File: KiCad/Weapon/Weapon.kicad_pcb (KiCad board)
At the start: 2 copper layers, 97.3 x 61 mm, 34 parts, among them IC1 ATMEGA328-P, J1 MICRO_USB, P1 2P_CGRID_M, P2 USB-TTL, P3 2P_CGRID_M, Q1 NPN, Q2 NPN, U1 MCP73831, U2 RFID-RC522, U3 LM1084IT-3.3/NOPB, X1 16MHz

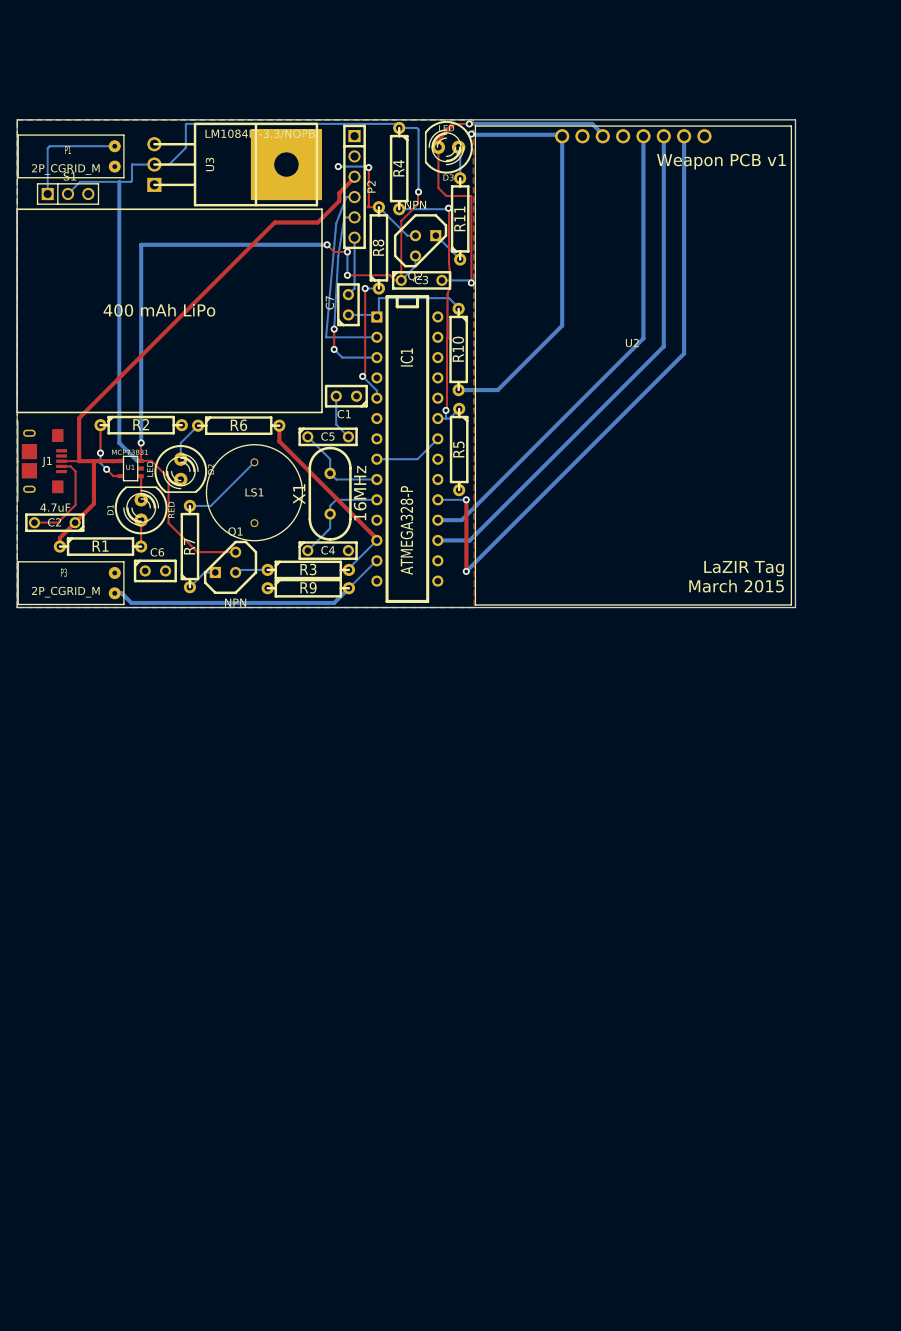
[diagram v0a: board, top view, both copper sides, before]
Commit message: Revert "3/29 KiCad Updates"
This reverts commit a2529da1b40b1f6e0e832ed1976ed3be41434859.
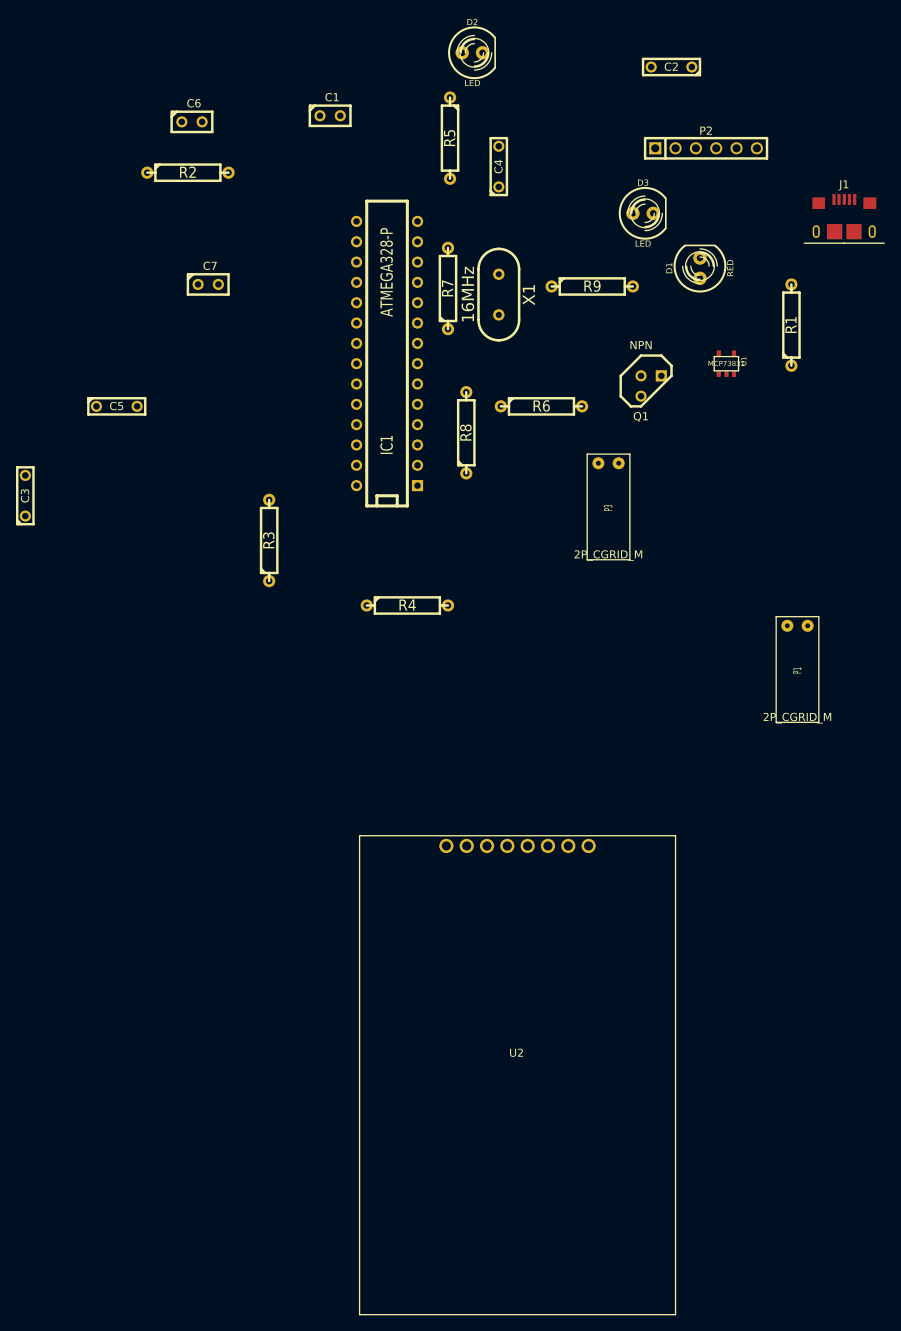
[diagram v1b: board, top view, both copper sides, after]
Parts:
- removed LS1: BUZZER, AI-1223Buzzer
- removed Q2: NPN, TO92
- removed R10: 10k, R4
- removed R11: 330, R4
- removed S1: SLIDESWITCH, PIN_ARRAY_3X1
- removed U3: LM1084IT-3.3/NOPB, TO220
- R3, R8: value 560 -> 10k
- R5: value 10k -> 1k
- R6: value 1k -> 560
- R7: value 330 -> 10k
- R9: value 10k -> 330
- moved J1 105.8 mm to (135.6, 37.8), turned to 0 degrees
- moved P1 103.6 mm to (129.8, 87.1), turned to 0 degrees
- moved C2 95.8 mm to (114.0, 17.3)
- moved R1 90.7 mm to (129.0, 49.5), turned to 90 degrees
- moved U2 89.9 mm to (114.6, 173.2)
- moved D1 76.1 mm to (117.6, 42.4)
- moved U1 75.6 mm to (120.9, 54.4), turned to 0 degrees
- moved D2 63.6 mm to (89.2, 15.5), turned to 0 degrees
- moved P3 63.5 mm to (106.2, 66.8), turned to 0 degrees
- moved Q1 57.6 mm to (111.5, 57.1), turned to 0 degrees
- moved C3 56.4 mm to (33.3, 70.9), turned to 90 degrees
- moved C6 56.3 mm to (54.1, 24.1)
- moved R4 54.6 mm to (81.0, 84.6), turned to 0 degrees
- moved C4 52.5 mm to (92.5, 29.7), turned to 90 degrees
- moved R9 51.8 mm to (104.1, 44.7)
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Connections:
- C3 pad 2: GND -> (no net)
- D2 pad 1: N-0000017 -> N-0000018
- IC1 pad 12: LED/Buzzer -> StatusLED
- P1 pad 2: N-000001 -> V-Bat
- Q1 pad 1: N-0000013 -> N-0000042
- Q1 pad 2: N-0000012 -> N-0000041
- R2 pad 2: GND -> (no net)
- R3 pad 1: N-0000012 -> V-Bat
- R3 pad 2: LED/Buzzer -> VoltageSense
- R4 pad 1: V-Bat -> VoltageSense
- R4 pad 2: VoltageSense -> GND
- R5 pad 1: VoltageSense -> N-0000018
- R5 pad 2: GND -> StatusLED
- R6 pad 1: N-0000017 -> LED-Driver
- R6 pad 2: LED/Buzzer -> N-0000041
- R7 pad 1: N-0000013 -> GND
- R7 pad 2: N-0000014 -> Trigger
- R8 pad 1: LED-Driver -> Reset
- R8 pad 2: N-0000042 -> +3.3V
- R9 pad 1: GND -> N-0000042
- R9 pad 2: Trigger -> N-0000043
- U1 pad 2: GND -> (no net)
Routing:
- net V-Bat: track 193.4 -> 0.00 mm, vias 5 -> 0
- net RFID-SCK: track 78.4 -> 0.00 mm, vias 2 -> 0
- net GND: track 74.3 -> 0.00 mm, vias 2 -> 0
- net USBV: track 72.8 -> 0.00 mm
- net RFID-MOSI: track 64.8 -> 0.00 mm
- net RFID-MISO: track 60.6 -> 0.00 mm
- net +3.3V: track 51.6 -> 0.00 mm, vias 1 -> 0
- net VoltageSense: track 36.0 -> 0.00 mm, vias 2 -> 0
- net Trigger: track 35.4 -> 0.00 mm
- net Uart-Rx: track 25.2 -> 0.00 mm
- net LED/Buzzer: track 24.5 -> 0.00 mm
- net Uart-Tx: track 23.6 -> 0.00 mm, vias 2 -> 0
- net Reset: track 16.7 -> 0.00 mm
- net N-0000042: track 16.3 -> 0.00 mm, vias 2 -> 0
- net LED-Driver: track 16.3 -> 0.00 mm, vias 2 -> 0
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- removed copper zone on B.Cu, net +3.3V
- removed copper zone on F.Cu, net GND
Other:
- board outline removed
- net class Default: trace_width 0.508 -> 0.254
- board text removed: "400 mAh LiPo"
- board text removed: "LaZIR Tag March 2015"
- board text removed: "Weapon PCB v1"
